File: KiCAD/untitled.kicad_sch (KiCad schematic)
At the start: 66 parts, among them J1 Power, J10 Conn_01x04, J11 Conn_01x04, J12 FDCAN_1, J13 FDCAN_2, J26 UART4, J5 Debug Header, J6 Conn_01x04, J7 Conn_01x04, J8 Conn_01x04, J9 Conn_01x04, SW1 PTS810SJM250SMTRLFS, SW2 PTS810SJM250SMTRLFS, SW3 PTS810SJM250SMTRLFS, SW4 PTS810SJM250SMTRLFS, SW5 SMQS-02R-TP, U1 STM32H573RIT6, U12 TPS7A2033DQNR, U5 USBLC6-2SC6, U7 MCP2562FD-E/P, U8 MCP2562FD-E/P, X1 SC-32S32.768kHz20PPM7pF, Y2 ECS-80-18-23B-JTM-TR

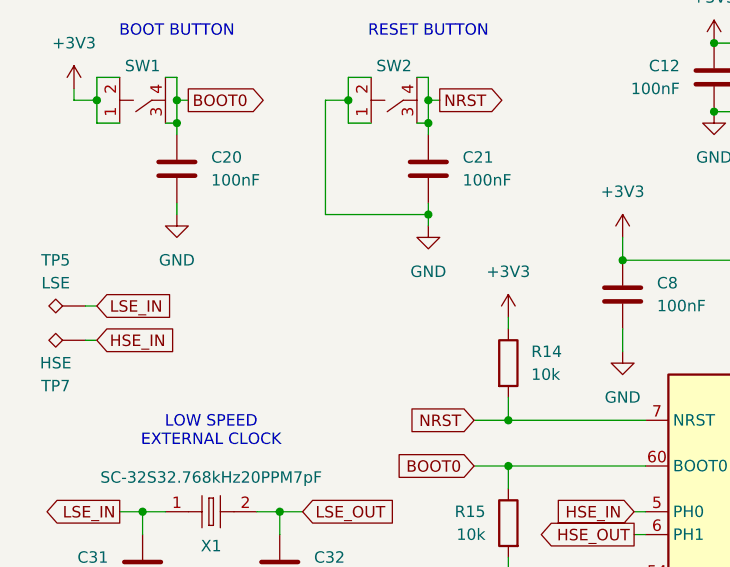
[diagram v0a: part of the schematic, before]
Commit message: Resolve DRC errors, cleanup traces, nudge footprints for hand soldering
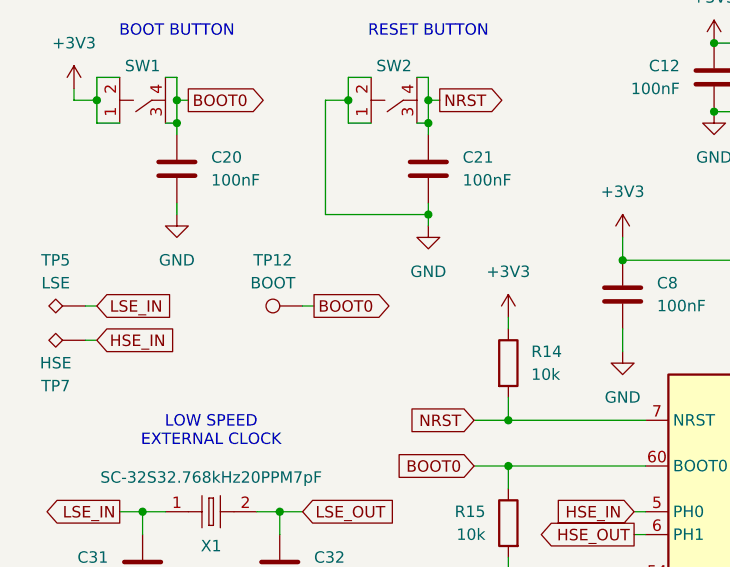
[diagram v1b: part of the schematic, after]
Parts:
- added TP12: BOOT, TestPoint:TestPoint_THTPad_D1.5mm_Drill0.7mm, symbol Connector:TestPoint
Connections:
- net BOOT0: now also TP12.1

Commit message: Fixed footprint libraries, corrected terminal block footprints, added 3d model for precharge resistor terminal block
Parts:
- added J27, J28: Screw_Terminal_01x03, easyeda2kicad:CONN-TH_3P-P3.50_OSTTE030161, symbol Connector:Screw_Terminal_01x03
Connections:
- net CANH_1: now also J27.3 (Pin_3)
- net CANH_2: now also J28.3 (Pin_3)
- net CANL_1: now also J27.1 (Pin_1)
- net CANL_2: now also J28.1 (Pin_1)
- net GND: now also J27.2 (Pin_2), J28.2 (Pin_2)
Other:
- moved on the sheet: J12
